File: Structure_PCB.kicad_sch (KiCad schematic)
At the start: 20 parts, among them J5 6620XX236022_662004236022, J6 6620XX236022_662004236022, J7 6620XX236022_662004236022, K2 FINDER-30.22

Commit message: finalized general layout
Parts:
- removed D1: 1N4148WT, Diode_SMD:D_SOD-523, symbol Diode:1N4148WT
- removed H13, H14: MountingHole, MountingHole:MountingHole_3.2mm_M3_DIN965_Pad, symbol Mechanical:MountingHole
- removed J5, J7: 6620XX236022_662004236022, Connector:662004236022, symbol Würth connectors:6620XX236022_662004236022
- added D4, D5, D6: ~, Diode_SMD:D_SOD-323, symbol Device:D_Schottky
- added J10, J12: JST-GH 4Pin, Connector_JST:JST_GH_SM04B-GHS-TB_1x04-1MP_P1.25mm_Horizontal, symbol Connector:Conn_01x04_Pin
- added J11: JST-GH 4Pin, Connector_JST:JST_GH_BM04B-GHS-TBT_1x04-1MP_P1.25mm_Vertical, symbol Connector:Conn_01x04_Pin
- added J9: Conn_02x04_Top_Bottom, Connector_Molex:Molex_Micro-Fit_3.0_43045-0800_2x04_P3.00mm_Horizontal, symbol Connector_Generic:Conn_02x04_Top_Bottom
- F1: value 3A -> 100 mA; footprint Fuse:Fuseholder_Cylinder-5x20mm_Wuerth_696103101002-SMD_Horizontal_Open -> Fuse:Fuse_0603_1608Metric_Pad1.05x0.95mm_HandSolder; Würth Nr.: 696103101002 -> (none)
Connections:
- net GND: now also D6.2 (A), J10.3 (Pin_3), J10.4 (Pin_4), J11.3 (Pin_3), J11.4 (Pin_4), J12.3 (Pin_3), J12.4 (Pin_4)
- net at F1.1: now also D4.1 (K), D5.1 (K)
- net at F1.2, J6.3, J6.4: now also J10.1 (Pin_1), J10.2 (Pin_2)
- net at K2.11, K2.21: now also J9.1 (Pin_1), J9.2 (Pin_2), J9.3 (Pin_3), J9.4 (Pin_4)
- net at K2.14, K2.24: now also J9.5 (Pin_5), J9.6 (Pin_6), J9.7 (Pin_7), J9.8 (Pin_8)
- net at J6.1, J6.2, K2.A1: now also D6.1 (K)
- new net: D5.2 (A), J11.1 (Pin_1), J11.2 (Pin_2)
- new net: D4.2 (A), J12.1 (Pin_1), J12.2 (Pin_2)
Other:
- note added: "2 in 1 out => power supply for arming (of own PB or other SB for redundancy)"
- note added: "<- GND"
- note added: "Mounting SB"
- note added: "SB"
- note added: "arming PB"
- note added: "to arming switch"
- moved on the sheet: F1, J6

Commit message: first prototype of SB finished
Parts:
- J11: footprint Connector_JST:JST_GH_BM04B-GHS-TBT_1x04-1MP_P1.25mm_Vertical -> Connector_JST:JST_GH_SM04B-GHS-TB_1x04-1MP_P1.25mm_Horizontal
- J6: footprint Connector:662004236022 -> stigma:Molex_Micro-Fit_3.0_43045-0400_2x02_P3.00mm_Horizontal
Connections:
- net HCout: now reaches J9.1 (Pin_1), J9.2 (Pin_2), J9.3 (Pin_3), J9.4 (Pin_4), K2.11, K2.21
- net HCin: now reaches J9.5 (Pin_5), J9.6 (Pin_6), J9.7 (Pin_7), J9.8 (Pin_8), K2.14, K2.24
- net pre_fuse: now reaches D4.1 (K), D5.1 (K), F1.1
- net SBout: now reaches F1.2, J10.1 (Pin_1), J10.2 (Pin_2), J6.3, J6.4
- net post_arm: now reaches D6.1 (K), J6.1, J6.2, K2.A1
- net PBin: now reaches D5.2 (A), J11.1 (Pin_1), J11.2 (Pin_2)
- net SBin: now reaches D4.2 (A), J12.1 (Pin_1), J12.2 (Pin_2)
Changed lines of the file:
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@@
+		)
+	)
+	(label "SBout"
+		(at 59.69 138.43 0)
+		(effects
+			(font
+				(size 1.27 1.27)
+			)
+			(justify left bottom)
+		)
+	)
+	(label "HCout"
+		(at 149.86 144.78 0)
+		(effects
+			(font
+				(size 1.27 1.27)
+			)
+			(justify left bottom)
+		)
+	)
+	(label "HCin"
+		(at 151.13 119.38 0)
+		(effects
+			(font
+				(size 1.27 1.27)
+			)
+			(justify left bottom)
+		)
+	)
+	(label "PBin"
+		(at 59.69 109.22 0)
+		(effects
+			(font
+				(size 1.27 1.27)
+			)
+			(justify left bottom)
+		)
+	)
+	(label "post_arm"
+		(at 110.49 124.46 0)
+		(effects
+			(font
+				(size 1.27 1.27)
+			)
+			(justify left bottom)
+		)
+	)
+	(label "pre_fuse"
+		(at 68.58 124.46 0)
+		(effects
+			(font
+				(size 1.27 1.27)
+			)
+			(justify left bottom)
+		)
+	)
+	(label "SBin"
+		(at 59.69 124.46 0)
+		(effects
+			(font
+				(size 1.27 1.27)
+			)
+			(justify left bottom)
 		)
 	)
@@
 			)
 		)
-		(property "Footprint" "Connector:662004236022"
+		(property "Footprint" "stigma:Molex_Micro-Fit_3.0_43045-0400_2x02_P3.00mm_Horizontal"
 			(at 109.22 115.57 0)
 			(effects
@@
 			)
 		)
-		(property "Footprint" "Connector_JST:JST_GH_BM04B-GHS-TBT_1x04-1MP_P1.25mm_Vertical"
+		(property "Footprint" "Connector_JST:JST_GH_SM04B-GHS-TB_1x04-1MP_P1.25mm_Horizontal"
 			(at 53.34 109.22 0)
 			(effects

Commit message: added cats vega mounting
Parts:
- added H13, H14, H15: MountingHole, MountingHole:MountingHole_3.2mm_M3_DIN965_Pad, symbol Mechanical:MountingHole
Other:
- note added: "Mounting CatsVega"
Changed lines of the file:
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@@
+		)
+	)
+	(text "Mounting CatsVega"
+		(exclude_from_sim no)
+		(at 207.518 62.738 0)
+		(effects
+			(font
+				(size 1.27 1.27)
+			)
 		)
 	)
@@
 	)
 	(symbol
+		(lib_id "Mechanical:MountingHole")
+		(at 200.66 67.31 0)
+		(unit 1)
+		(exclude_from_sim yes)
+		(in_bom no)
+		(on_board yes)
+		(dnp no)
+		(fields_autoplaced yes)
+		(property "Reference" "H13"
+			(at 203.2 66.0399 0)
+			(effects
+				(font
+					(size 1.27 1.27)
+				)
+				(justify left)
+			)
+		)
+		(property "Value" "MountingHole"
+			(at 203.2 68.5799 0)
+			(effects
+				(font
+					(size 1.27 1.27)
+				)
+				(justify left)
+			)
+		)
+		(property "Footprint" "MountingHole:MountingHole_3.2mm_M3_DIN965_Pad"
+			(at 200.66 67.31 0)
+			(effects
+				(font
+					(size 1.27 1.27)
+				)
+				(hide yes)
+			)
+		)
+		(property "Datasheet" "~"
+			(at 200.66 67.31 0)
+			(effects
+				(font
+					(size 1.27 1.27)
+				)
+				(hide yes)
+			)
+		)
+		(property "Description" "Mounting Hole without connection"
+			(at 200.66 67.31 0)
+			(effects
+				(font
+					(size 1.27 1.27)
+				)
+				(hide yes)
+			)
+		)
+		(instances
+			(project "Structure_PCB"
+				(path "/6b5e11c5-042c-4871-8828-d1d1e7f237a0"
+					(reference "H13")
+					(unit 1)
+				)
+			)
+		)
+	)
+	(symbol
 		(lib_id "Device:D_Schottky")
 		(at 63.5 124.46 180)
@@
 	)
 	(symbol
+		(lib_id "Mechanical:MountingHole")
+		(at 200.66 80.01 0)
+		(unit 1)
+		(exclude_from_sim yes)
+		(in_bom no)
+		(on_board yes)
+		(dnp no)
+		(fields_autoplaced yes)
+		(property "Reference" "H15"
+			(at 203.2 78.7399 0)
+			(effects
+				(font
+					(size 1.27 1.27)
+				)
+				(justify left)
+			)
+		)
+		(property "Value" "MountingHole"
+			(at 203.2 81.2799 0)
+			(effects
+				(font
+					(size 1.27 1.27)
+				)
+				(justify left)
+			)
+		)
+		(property "Footprint" "MountingHole:MountingHole_3.2mm_M3_DIN965_Pad"
+			(at 200.66 80.01 0)
+			(effects
+				(font
+					(size 1.27 1.27)
+				)
+				(hide yes)
+			)
+		)
+		(property "Datasheet" "~"
+			(at 200.66 80.01 0)
+			(effects
+				(font
+					(size 1.27 1.27)
+				)
+				(hide yes)
+			)
+		)
+		(property "Description" "Mounting Hole without connection"
+			(at 200.66 80.01 0)
+			(effects
+				(font
+					(size 1.27 1.27)
+				)
+				(hide yes)
+			)
+		)
+		(instances
+			(project "Structure_PCB"
+				(path "/6b5e11c5-042c-4871-8828-d1d1e7f237a0"
+					(reference "H15")
+					(unit 1)
+				)
+			)
+		)
+	)
+	(symbol
 		(lib_id "Device:D_Schottky")
 		(at 120.65 133.35 270)
@@
 					(unit 1)
 				)
+			)
+		)
+	)
+	(symbol
+		(lib_id "Mechanical:MountingHole")
+		(at 200.66 73.66 0)
+		(unit 1)
+		(exclude_from_sim yes)
+		(in_bom no)
+		(on_board yes)
+		(dnp no)
+		(fields_autoplaced yes)
+		(property "Reference" "H14"
+			(at 203.2 72.3899 0)
+			(effects
+				(font
+					(size 1.27 1.27)
+				)
+				(justify left)
+			)
+		)
+		(property "Value" "MountingHole"
+			(at 203.2 74.9299 0)
+			(effects
+				(font
+					(size 1.27 1.27)
+				)
+				(justify left)
+			)
+		)
+		(property "Footprint" "MountingHole:MountingHole_3.2mm_M3_DIN965_Pad"
+			(at 200.66 73.66 0)
+			(effects
+				(font
+					(size 1.27 1.27)
+				)
+				(hide yes)
+			)
+		)
+		(property "Datasheet" "~"
+			(at 200.66 73.66 0)
+			(effects
+				(font
+					(size 1.27 1.27)
+				)
+				(hide yes)
+			)
+		)
+		(property "Description" "Mounting Hole without connection"
+			(at 200.66 73.66 0)
+			(effects
+				(font
+					(size 1.27 1.27)
+				)
+				(hide yes)
+			)
+		)
+		(instances
+			(project "Structure_PCB"
+				(path "/6b5e11c5-042c-4871-8828-d1d1e7f237a0"
+					(reference "H14")
+					(unit 1)
+				)

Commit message: added correct footprint vor vega mount
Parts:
- H13, H14, H15: footprint MountingHole:MountingHole_3.2mm_M3_DIN965_Pad -> Mounting_Wuerth:Mounting_Wuerth_WA-SMSR-3.2mm_H4.6mm_ReverseMount_9775046960
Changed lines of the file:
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@@
 			)
 		)
-		(property "Footprint" "MountingHole:MountingHole_3.2mm_M3_DIN965_Pad"
+		(property "Footprint" "Mounting_Wuerth:Mounting_Wuerth_WA-SMSR-3.2mm_H4.6mm_ReverseMount_9775046960"
 			(at 200.66 67.31 0)
 			(effects
@@
 			)
 		)
-		(property "Footprint" "MountingHole:MountingHole_3.2mm_M3_DIN965_Pad"
+		(property "Footprint" "Mounting_Wuerth:Mounting_Wuerth_WA-SMSR-3.2mm_H4.6mm_ReverseMount_9775046960"
 			(at 200.66 80.01 0)
 			(effects
@@
 			)
 		)
-		(property "Footprint" "MountingHole:MountingHole_3.2mm_M3_DIN965_Pad"
+		(property "Footprint" "Mounting_Wuerth:Mounting_Wuerth_WA-SMSR-3.2mm_H4.6mm_ReverseMount_9775046960"
 			(at 200.66 73.66 0)
 			(effects

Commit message: most recent changes to layout, changed some components for hand soldering
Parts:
- D4, D5, D6: footprint Diode_SMD:D_SOD-323 -> Diode_SMD:D_SOD-123F; LCSC C191023 -> C167645
- F1: footprint Fuse:Fuse_0603_1608Metric_Pad1.05x0.95mm_HandSolder -> Fuse:Fuse_1206_3216Metric_Pad1.42x1.75mm_HandSolder
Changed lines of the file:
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@@
 			)
 		)
-		(property "Footprint" "Fuse:Fuse_0603_1608Metric_Pad1.05x0.95mm_HandSolder"
+		(property "Footprint" "Fuse:Fuse_1206_3216Metric_Pad1.42x1.75mm_HandSolder"
 			(at 72.39 110.998 90)
 			(effects
@@
 			)
 		)
-		(property "Footprint" "Diode_SMD:D_SOD-323"
+		(property "Footprint" "Diode_SMD:D_SOD-123F"
 			(at 63.5 109.22 0)
 			(effects
@@
 			)
 		)
-		(property "LCSC" "C191023"
+		(property "LCSC" "C167645"
 			(at 63.5 109.22 0)
 			(effects
@@
 			)
 		)
-		(property "Footprint" "Diode_SMD:D_SOD-323"
+		(property "Footprint" "Diode_SMD:D_SOD-123F"
 			(at 63.5 124.46 0)
 			(effects
@@
 			)
 		)
-		(property "LCSC" "C191023"
+		(property "LCSC" "C167645"
 			(at 63.5 124.46 0)
 			(effects
@@
 			)
 		)
-		(property "Footprint" "Diode_SMD:D_SOD-323"
+		(property "Footprint" "Diode_SMD:D_SOD-123F"
 			(at 120.65 133.35 0)
 			(effects
@@
 			)
 		)
-		(property "LCSC" "C191023"
+		(property "LCSC" "C167645"
 			(at 120.65 133.35 0)
 			(effects

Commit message: changes to layout, added EB
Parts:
- added H16, H17, H18, H19: MountingHole, Mounting_Wuerth:Mounting_Wuerth_WA-SMSR-3.2mm_H4.6mm_ReverseMount_9775046960, symbol Mechanical:MountingHole
- added HS10, HS11, HS12, HS13, HS14, HS15, HS16, HS17, HS18, HS19, HS20, HS21, HS22, HS23, HS24, HS25, HS26, HS27, HS28, HS29, HS30, HS31, HS32, HS33, HS34, HS35, HS36, HS37, HS42, HS43, HS44, HS45, HS46, HS47, HS48, HS49, HS50, HS51, HS52, HS53, HS54, HS55, HS56, HS57, HS58, HS59, HS60, HS61, HS62, HS63, HS64, HS65, HS66, HS67, HS68, HS69, HS70, HS71, HS72, HS73, HS74, HS75, HS76, HS77, HS78, HS79, HS80, HS81, HS82, HS83, HS84, HS9: Heatsink_Pad, Heatsink:würth 5x5 heat pads, symbol Mechanical:Heatsink_Pad
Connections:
- net GND: now also HS10.1, HS11.1, HS12.1, HS13.1, HS14.1, HS15.1, HS16.1, HS17.1, HS18.1, HS19.1, HS20.1, HS21.1, HS22.1, HS23.1, HS24.1, HS25.1, HS26.1, HS27.1, HS28.1, HS29.1, HS30.1, HS31.1, HS32.1, HS33.1, HS34.1, HS35.1, HS36.1, HS37.1, HS42.1, HS43.1, HS44.1, HS45.1, HS46.1, HS47.1, HS48.1, HS49.1, HS50.1, HS51.1, HS52.1, HS53.1, HS54.1, HS55.1, HS56.1, HS57.1, HS58.1, HS59.1, HS60.1, HS61.1, HS62.1, HS63.1, HS64.1, HS65.1, HS66.1, HS67.1, HS68.1, HS69.1, HS70.1, HS71.1, HS72.1, HS73.1, HS74.1, HS75.1, HS76.1, HS77.1, HS78.1, HS79.1, HS80.1, HS81.1, HS82.1, HS83.1, HS84.1, HS9.1
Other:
- note added: "Mounting EB"
- moved on the sheet: D4, D5, D6, F1, J10, J11, J12, J6, J9, K2

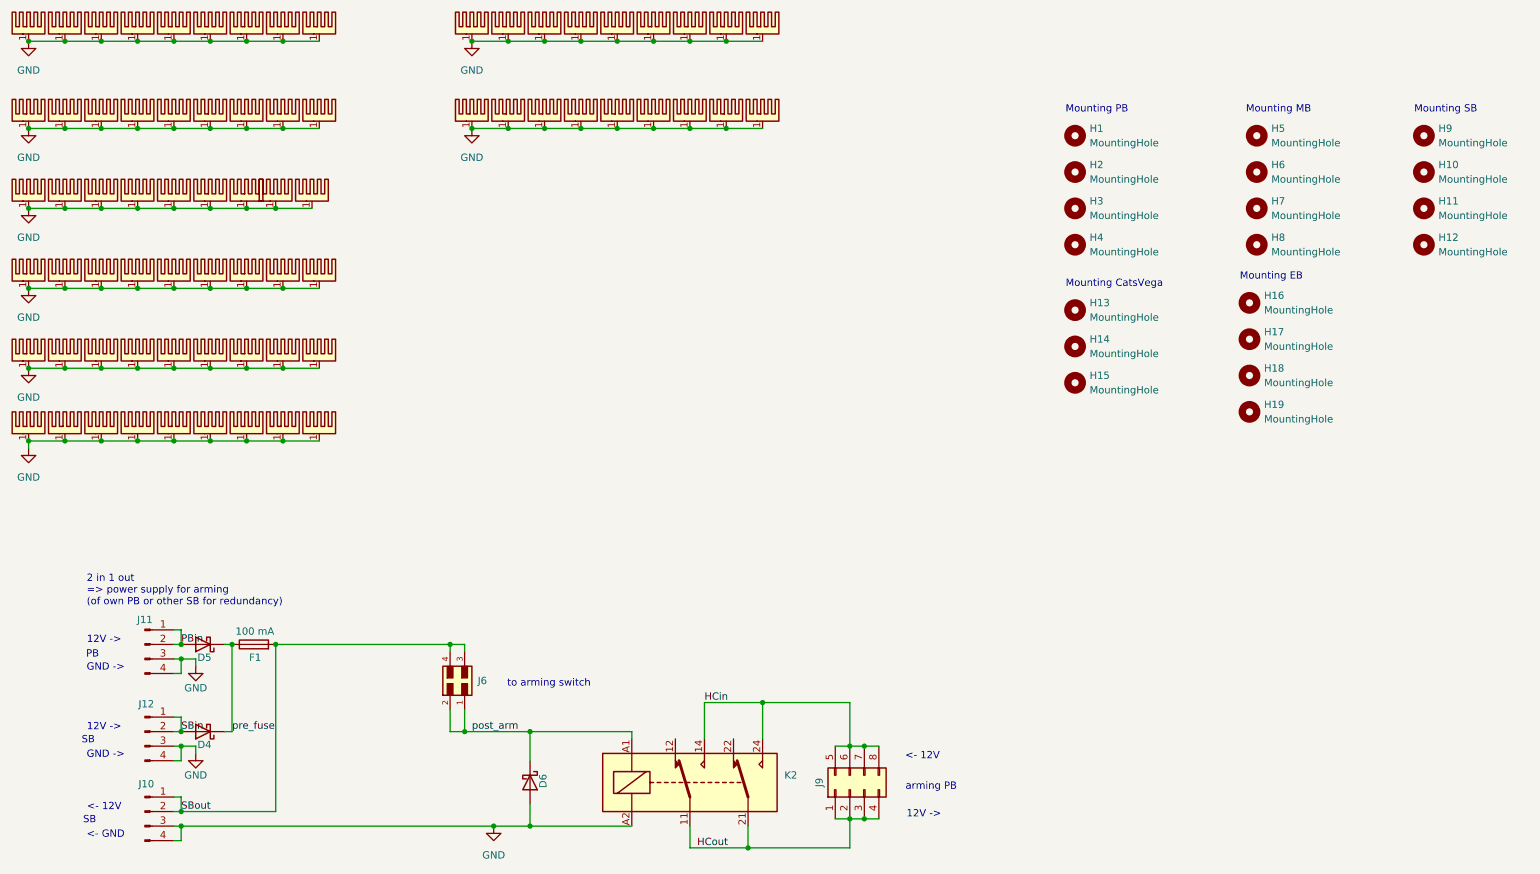
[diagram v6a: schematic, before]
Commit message: added some thermal pads
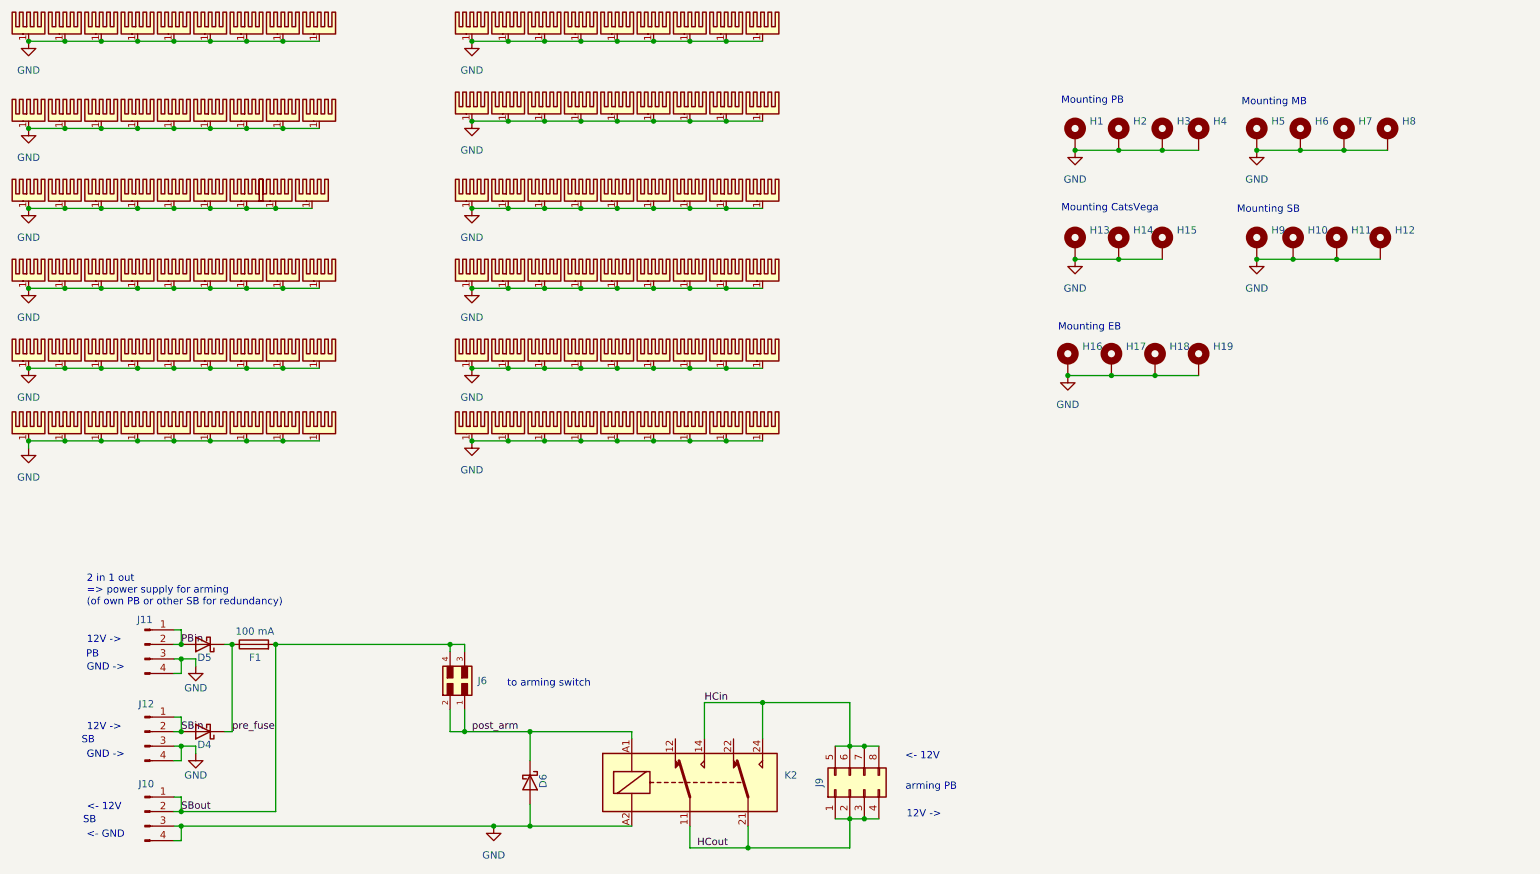
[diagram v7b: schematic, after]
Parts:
- added HS100, HS101, HS102, HS103, HS104, HS105, HS106, HS107, HS108, HS109, HS110, HS111, HS112, HS113, HS114, HS115, HS116, HS117, HS118, HS119, HS120, HS85, HS86, HS87, HS88, HS89, HS90, HS91, HS92, HS93, HS94, HS95, HS96, HS97, HS98, HS99: Heatsink_Pad, Heatsink:würth 5x5 heat pads, symbol Mechanical:Heatsink_Pad
- H1, H10, H11, H12, H13, H14, H15, H16, H17, H18, H19, H2, H3, H4, H5, H6, H7, H8, H9: value MountingHole -> MountingHole_Pad; symbol Mechanical:MountingHole -> Mechanical:MountingHole_Pad
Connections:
- net GND: now also H1.1, H10.1, H11.1, H12.1, H13.1, H14.1, H15.1, H16.1, H17.1, H18.1, H19.1, H2.1, H3.1, H4.1, H5.1, H6.1, H7.1, H8.1, H9.1, HS100.1, HS101.1, HS102.1, HS103.1, HS104.1, HS105.1, HS106.1, HS107.1, HS108.1, HS109.1, HS110.1, HS111.1, HS112.1, HS113.1, HS114.1, HS115.1, HS116.1, HS117.1, HS118.1, HS119.1, HS120.1, HS85.1, HS86.1, HS87.1, HS88.1, HS89.1, HS90.1, HS91.1, HS92.1, HS93.1, HS94.1, HS95.1, HS96.1, HS97.1, HS98.1, HS99.1

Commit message: Fix relay footprint, correct zones, round off through trace
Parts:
- K2: value FINDER-30.22 -> FINDER-40.61; footprint Relay_THT:Relay_DPDT_Finder_30.22 -> Relay_THT:Relay_SPDT_Finder_40.61
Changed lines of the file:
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@@
 			)
 		)
-		(property "Value" "FINDER-30.22"
+		(property "Value" "FINDER-40.61"
 			(at 149.86 151.1299 0)
 			(effects
@@
 			)
 		)
-		(property "Footprint" "Relay_THT:Relay_DPDT_Finder_30.22"
+		(property "Footprint" "Relay_THT:Relay_SPDT_Finder_40.61"
 			(at 167.64 150.622 0)
 			(effects
